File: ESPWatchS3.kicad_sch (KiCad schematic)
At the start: 137 parts

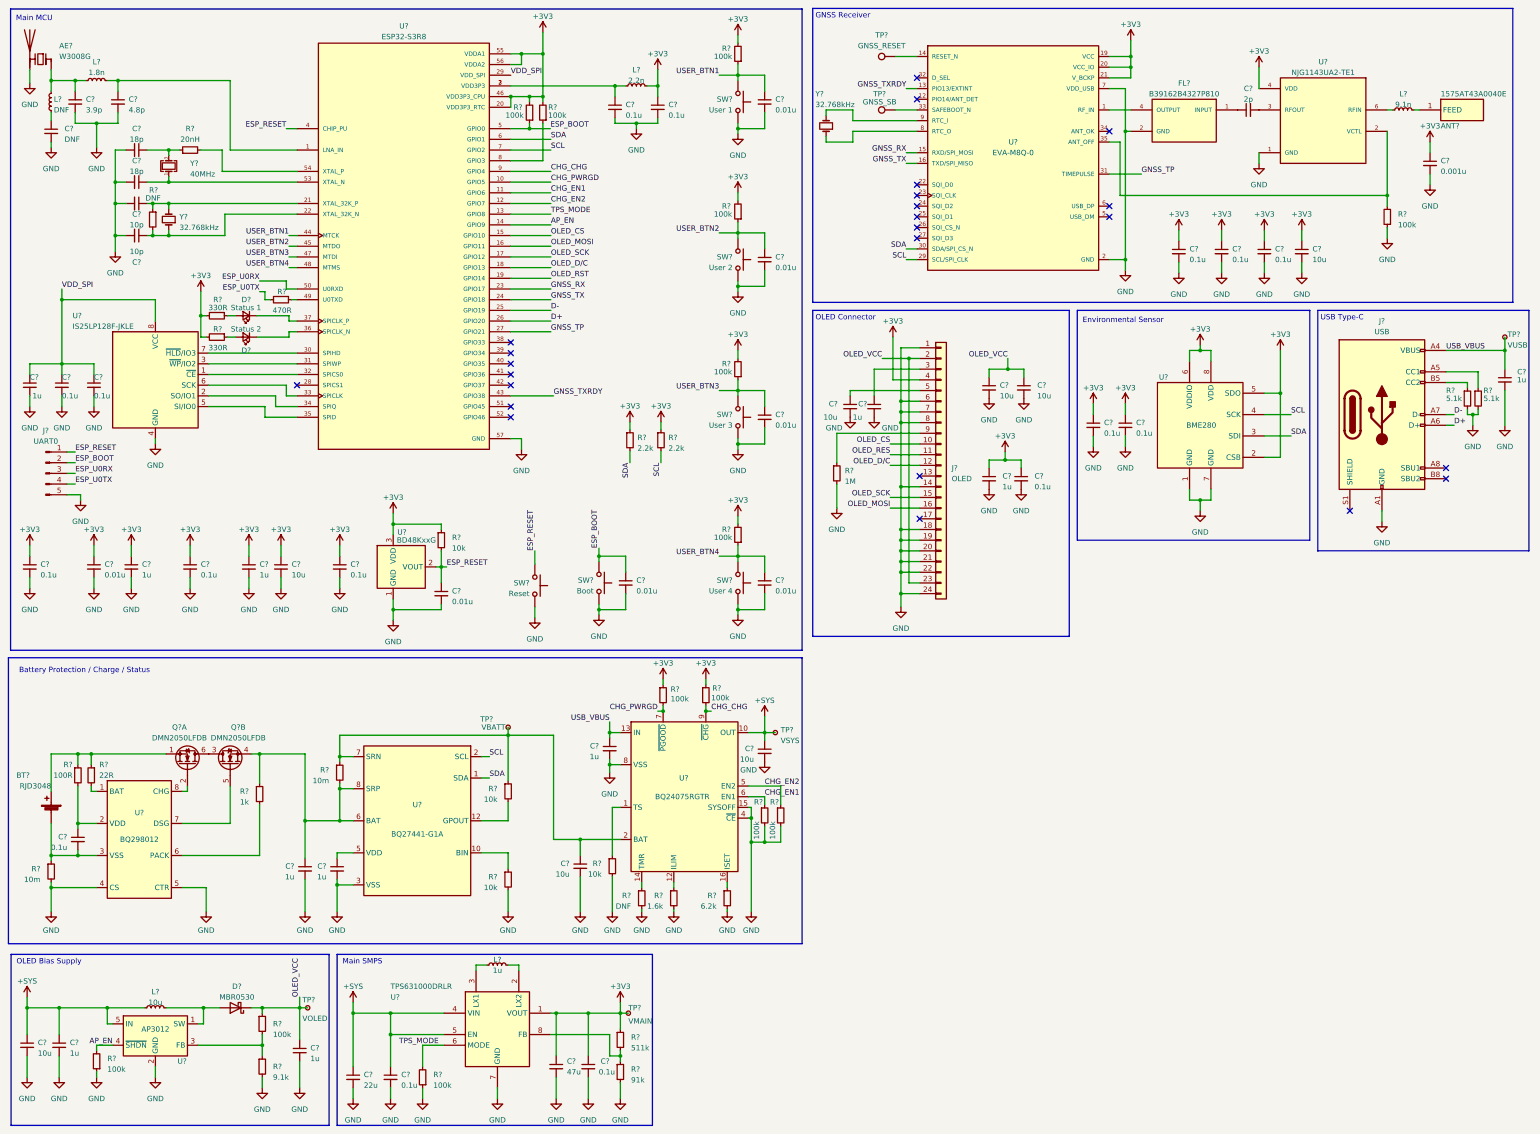
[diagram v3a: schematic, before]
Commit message: Initial annotation, and added OLED VDD Jumper
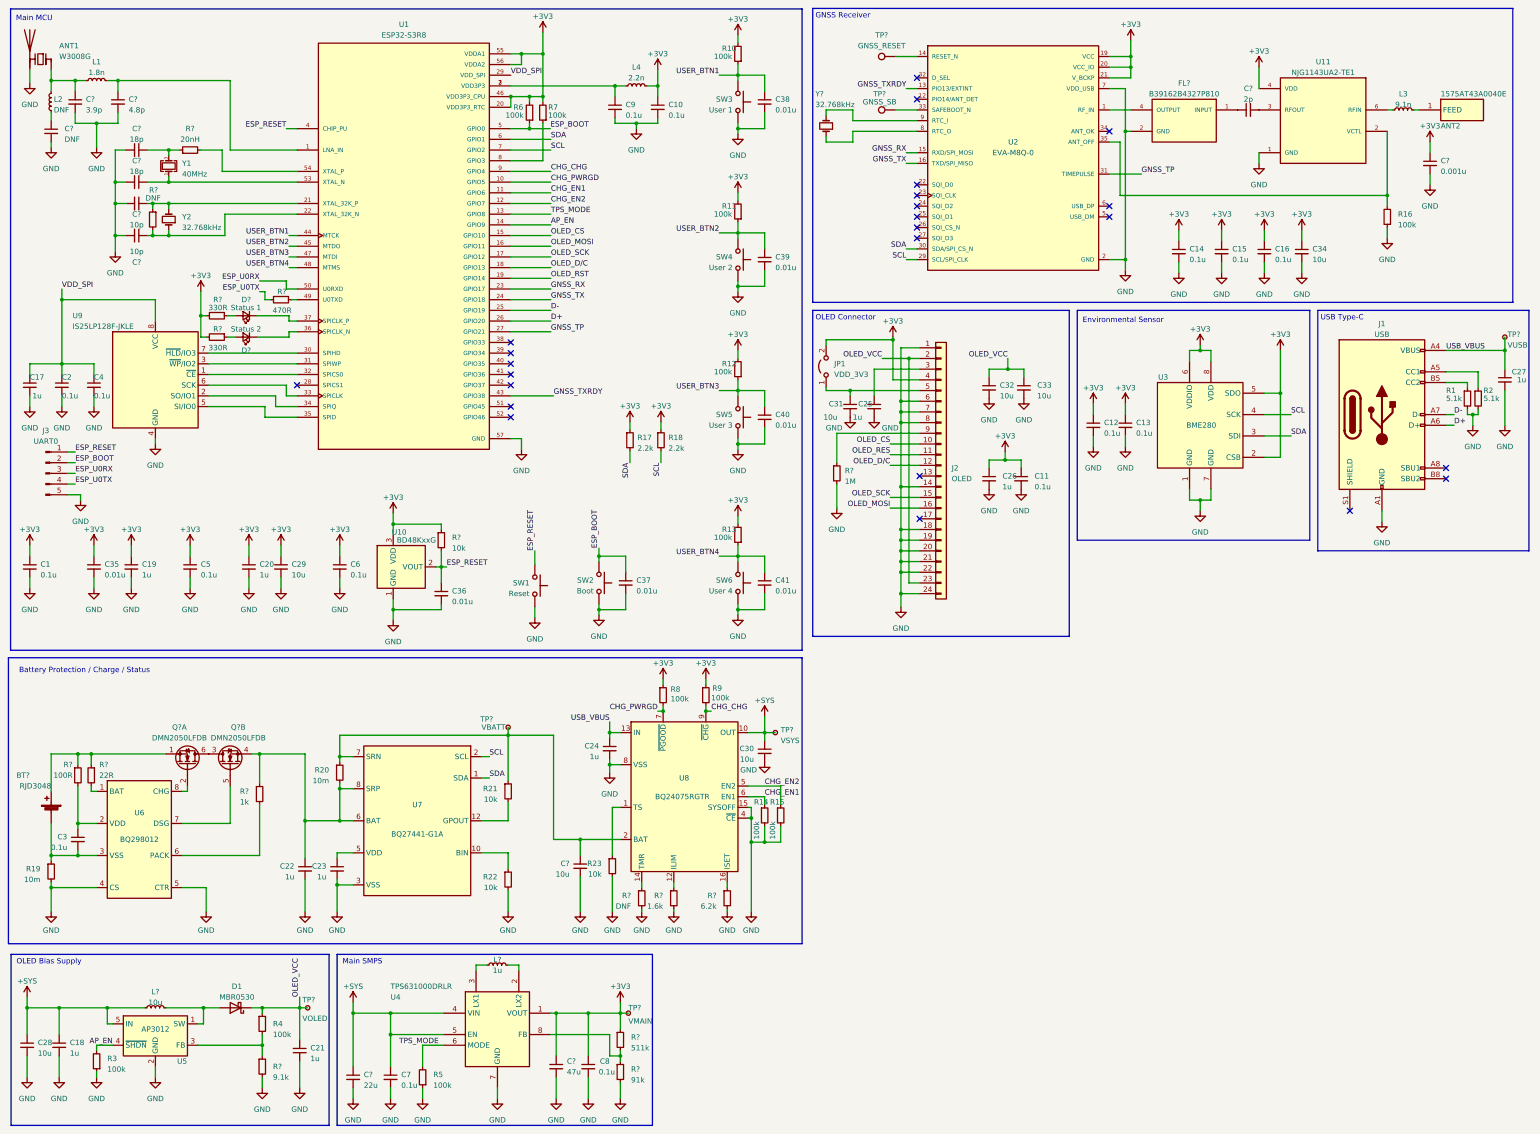
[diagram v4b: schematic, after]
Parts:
- added JP1: VDD_3V3, symbol Jumper:Jumper_2_Open
- gave numbers to parts that had none: 93
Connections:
- net +3V3: now also JP1.2 (B)
- net at C31.1, J2.5 (Pin_5): now also JP1.1 (A)

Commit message: Initial footprint assignments
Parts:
- BT1: renamed from BT?; footprint (none) -> WatchParts:BAT_3046
- gave numbers to parts that had none: 42
- renumbered C35 to C42

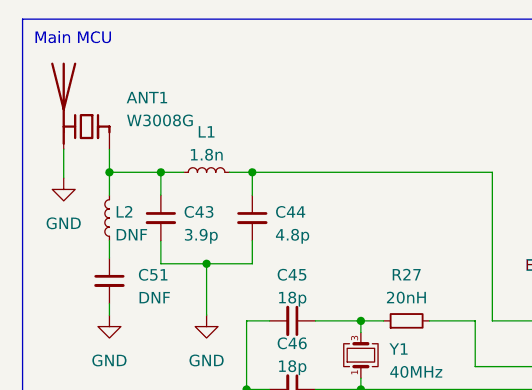
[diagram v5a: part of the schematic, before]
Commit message: Finish part footprint assignment
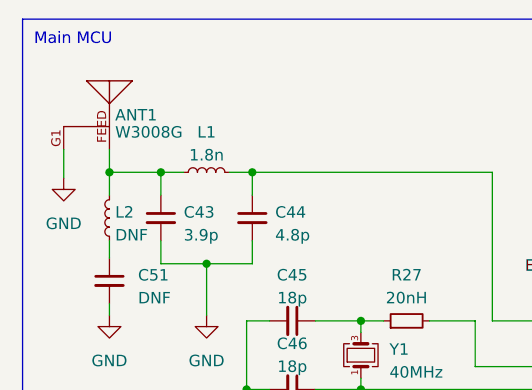
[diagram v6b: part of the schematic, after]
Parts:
- removed ANT1: W3008G, symbol Device:Antenna_Chip
- added ANT1: W3008G, WatchParts:ANTENNA_W3008, symbol WatchParts:W3008G
- C1, C10, C11, C12, C13, C14, C15, C16, C2, C3, C36, C37, C38, C39, C4, C40, C41, C42, C43, C44, C45, C46, C47, C48, C5, C51, C52, C53, C6, C7, C8, C9: footprint (none) -> Capacitor_SMD:C_0402_1005Metric
- C17, C18, C19, C20, C21, C22, C23, C24, C25, C26, C27: footprint (none) -> Capacitor_SMD:C_0603_1608Metric
- C28, C29, C30, C31, C32, C33, C34, C35, C49, C50: footprint (none) -> Capacitor_SMD:C_0805_2012Metric
- D2, D3: footprint (none) -> LED_SMD:LED_0603_1608Metric
- J3: footprint (none) -> Connector_PinHeader_2.54mm:PinHeader_1x05_P2.54mm_Vertical
- JP1: footprint (none) -> Jumper:SolderJumper-2_P1.3mm_Open_RoundedPad1.0x1.5mm
- L1, L2, L3, L4: footprint (none) -> Inductor_SMD:L_0402_1005Metric
- L5: footprint WatchParts:SRP2512TMA1R0M -> Inductor_SMD:L_1008_2520Metric
- Q1: footprint https://www.diodes.com/assets/Datasheets/DMN2050LFDB.pdf -> WatchParts:MOSFET_DMP2160UFDB-7
- R1, R10, R11, R12, R13, R14, R15, R16, R17, R18, R2, R21, R22, R23, R24, R25, R26, R27, R28, R29, R3, R30, R31, R32, R33, R34, R35, R36, R37, R38, R39, R4, R5, R6, R7, R8, R9: footprint (none) -> Resistor_SMD:R_0402_1005Metric
- R19, R20: footprint (none) -> Resistor_SMD:R_0805_2012Metric
- TP1, TP2, TP3, TP4, TP5, TP6, TP7: footprint (none) -> TestPoint:TestPoint_Pad_D1.5mm
- Y2, Y3: footprint (none) -> Crystal:Crystal_SMD_3215-2Pin_3.2x1.5mm
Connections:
- net EP: now also ANT1.G1, ANT1.G2
- net at C43.1, L1.1, L2.2: now also ANT1.FEED

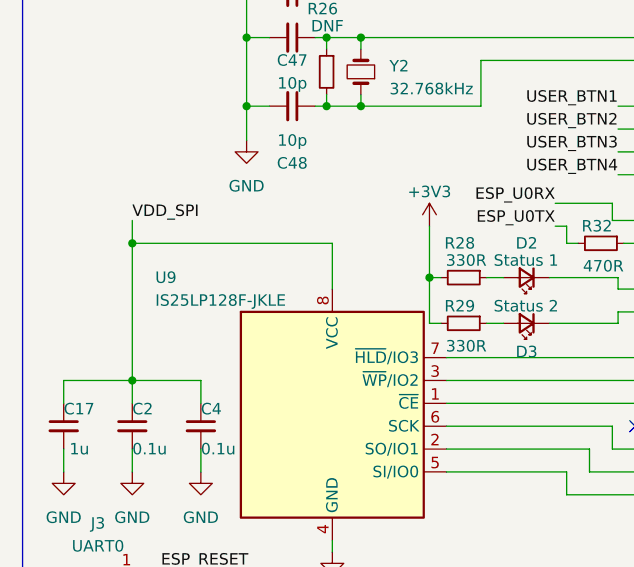
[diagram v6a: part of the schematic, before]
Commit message: Partially fixed schematic symbols missing pins
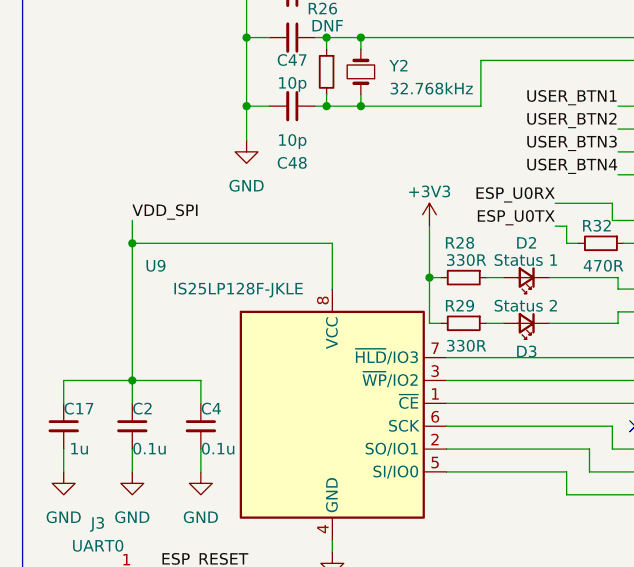
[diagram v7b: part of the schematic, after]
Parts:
- removed U9: IS25LP128F-JKLE, Package_SON:WSON-8-1EP_6x5mm_P1.27mm_EP3.4x4mm, symbol WatchParts:IS25WP128F-JKLE
- added U9: IS25LP128F-JKLE, Package_SON:WSON-8-1EP_6x5mm_P1.27mm_EP3.4x4mm, symbol WatchParts:IS25LP128F-JKLE
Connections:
- net EP: now also U7.13 (EP), U9.4 (GND), U9.9 (EP)
- net VDD_SPI: now also U9.8 (VCC)
- net at C3.2, R19.1, U6.3 (VSS): now also BT1.N (-); no longer BT1.2 (-)
- net at Q1.1 (S), R24.1, R25.1: now also BT1.P1 (+), BT1.P2 (+); no longer BT1.1 (+)
- net at U1.30 (SPIHD): now also U9.7 (~{HLD}/IO3)
- net at U1.31 (SPIWP): now also U9.3 (~{WP}/IO2)
- net at U1.32 (SPICS0): now also U9.1 (~{CE})
- net at U1.33 (SPICLK): now also U9.6 (SCK)
- net at U1.34 (SPIQ): now also U9.2 (SO/IO1)
- net at U1.35 (SPID): now also U9.5 (SI/IO0)
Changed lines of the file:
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@@
       (effects (font (size 1.27 1.27)) (justify left))
     )
-    (property "Footprint" "WatchParts:BAT_3046" (at 23.495 203.581 90)
+    (property "Footprint" "WatchParts:BAT_3046" (at 23.495 205.105 90)
       (effects (font (size 1.27 1.27)) hide)
     )
@@
       (effects (font (size 1.27 1.27)) hide)
     )
-    (pin "1")
-    (pin "2")
+    (pin "N")
+    (pin "P1")
+    (pin "P2")
     (instances
       (project "ESPWatchS3"
@@
     )
   )
-  (symbol (lib_id "WatchParts:IS25WP128F-JKLE") (at 48.26 100.965 0) (unit 1)
-    (in_bom yes) (on_board yes) (dnp no)
-    (property "Reference" "U9" (at 28.575 86.995 0)
-      (effects (font (size 1.27 1.27)) (justify left))
-    )
-    (property "Value" "IS25LP128F-JKLE" (at 28.575 89.535 0)
-      (effects (font (size 1.27 1.27)) (justify left))
-    )
-    (property "Footprint" "Package_SON:WSON-8-1EP_6x5mm_P1.27mm_EP3.4x4mm" (at 49.53 85.725 0)
-      (effects (font (size 1.27 1.27)) hide)
-    )
-    (property "Datasheet" "https://www.mouser.com/datasheet/2/198/25LP_WP128F-1146765.pdf" (at 49.53 113.665 0)
-      (effects (font (size 1.27 1.27)) hide)
-    )
-    (pin "1")
-    (pin "2")
-    (pin "3")
-    (pin "4")
-    (pin "5")
-    (pin "6")
-    (pin "7")
-    (pin "8")
-    (instances
-      (project "ESPWatchS3"
-        (path "/bf5b2c41-bb33-4360-ba29-22d569e03292"
-          (reference "U9") (unit 1)
-        )
-      )
-    )
-  )
   (symbol (lib_id "power:GND") (at 18.415 108.585 0) (unit 1)
     (in_bom yes) (on_board yes) (dnp no) (fields_autoplaced)
@@
     (pin "11")
     (pin "12")
+    (pin "13")
     (pin "2")
     (pin "3")
@@
         )
       )
+    )
+  )
+  (symbol (lib_id "WatchParts:IS25LP128F-JKLE") (at 48.26 100.965 0) (unit 1)
+    (in_bom yes) (on_board yes) (dnp no)
+    (property "Reference" "U9" (at 29.845 85.725 0)
+      (effects (font (size 1.27 1.27)) (justify right))
+    )
+    (property "Value" "IS25LP128F-JKLE" (at 45.085 88.265 0)
+      (effects (font (size 1.27 1.27)) (justify right))
+    )
+    (property "Footprint" "Package_SON:WSON-8-1EP_6x5mm_P1.27mm_EP3.4x4mm" (at 49.53 85.725 0)
+      (effects (font (size 1.27 1.27)) hide)
+    )
+    (property "Datasheet" "https://www.mouser.com/datasheet/2/198/25LP_WP128F-1146765.pdf" (at 49.53 113.665 0)
+      (effects (font (size 1.27 1.27)) hide)
+    )
+    (pin "1")
+    (pin "2")
+    (pin "3")
+    (pin "4")
+    (pin "5")
+    (pin "6")
+    (pin "7")
+    (pin "8")
+    (pin "9")
+    (instances
+      (project "ESPWatchS3"
+        (path "/bf5b2c41-bb33-4360-ba29-22d569e03292"
+          (reference "U9") (unit 1)
+        )
+      )

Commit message: Fixed footprints, dumped parts into PCB layout
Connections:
- net ESP_BOOT: now also SW2.3; no longer SW2.2
- net ESP_RESET: now also SW1.3; no longer SW1.2
- net USER_BTN1: now also SW3.3; no longer SW3.2
- net USER_BTN2: now also SW4.3; no longer SW4.2
- net USER_BTN3: now also SW5.3; no longer SW5.2
- net USER_BTN4: now also SW6.3; no longer SW6.2
- net at Q1.3 (D), Q1.6 (D): now also Q1.7 (D), Q1.8 (D)
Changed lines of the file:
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@@
     (pin "1")
     (pin "2")
-    (pin "2")
+    (pin "3")
     (pin "4")
     (instances
@@
     )
   )
-  (symbol (lib_id "WatchParts:PTS815") (at 153.67 150.495 270) (mirror x) (unit 1)
+  (symbol (lib_name "PTS815_5") (lib_id "WatchParts:PTS815") (at 153.67 150.495 270) (mirror x) (unit 1)
     (in_bom yes) (on_board yes) (dnp no)
     (property "Reference" "SW2" (at 152.4 149.86 90)
@@
     (pin "1")
     (pin "2")
-    (pin "2")
+    (pin "3")
     (pin "4")
     (instances
@@
     (pin "2")
     (pin "6")
+    (pin "7")
     (pin "3")
     (pin "4")
     (pin "5")
+    (pin "8")
     (instances
       (project "ESPWatchS3"
@@
     (pin "2")
     (pin "6")
+    (pin "7")
     (pin "3")
     (pin "4")
     (pin "5")
+    (pin "8")
     (instances
       (project "ESPWatchS3"
@@
     )
   )
-  (symbol (lib_id "WatchParts:PTS815") (at 186.69 111.125 270) (mirror x) (unit 1)
+  (symbol (lib_name "PTS815_3") (lib_id "WatchParts:PTS815") (at 186.69 111.125 270) (mirror x) (unit 1)
     (in_bom yes) (on_board yes) (dnp no)
     (property "Reference" "SW5" (at 185.42 110.49 90)
@@
     (pin "1")
     (pin "2")
-    (pin "2")
+    (pin "3")
     (pin "4")
     (instances
@@
     )
   )
-  (symbol (lib_id "WatchParts:PTS815") (at 186.69 36.195 270) (mirror x) (unit 1)
+  (symbol (lib_name "PTS815_1") (lib_id "WatchParts:PTS815") (at 186.69 36.195 270) (mirror x) (unit 1)
     (in_bom yes) (on_board yes) (dnp no)
     (property "Reference" "SW3" (at 185.42 35.56 90)
@@
     (pin "1")
     (pin "2")
-    (pin "2")
+    (pin "3")
     (pin "4")
     (instances
@@
     )
   )
-  (symbol (lib_id "WatchParts:PTS815") (at 186.69 150.495 270) (mirror x) (unit 1)
+  (symbol (lib_name "PTS815_4") (lib_id "WatchParts:PTS815") (at 186.69 150.495 270) (mirror x) (unit 1)
     (in_bom yes) (on_board yes) (dnp no)
     (property "Reference" "SW6" (at 185.42 149.86 90)
@@
     (pin "1")
     (pin "2")
-    (pin "2")
+    (pin "3")
     (pin "4")
     (instances
@@
     )
   )
-  (symbol (lib_id "WatchParts:PTS815") (at 186.69 73.66 270) (mirror x) (unit 1)
+  (symbol (lib_name "PTS815_2") (lib_id "WatchParts:PTS815") (at 186.69 73.66 270) (mirror x) (unit 1)
     (in_bom yes) (on_board yes) (dnp no)
     (property "Reference" "SW4" (at 185.42 73.025 90)
@@
     (pin "1")
     (pin "2")
-    (pin "2")
+    (pin "3")
     (pin "4")
     (instances
